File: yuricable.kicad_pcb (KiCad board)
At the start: 2 copper layers, 66.1 x 29.1 mm, 34 parts, among them U1 FlipperZero

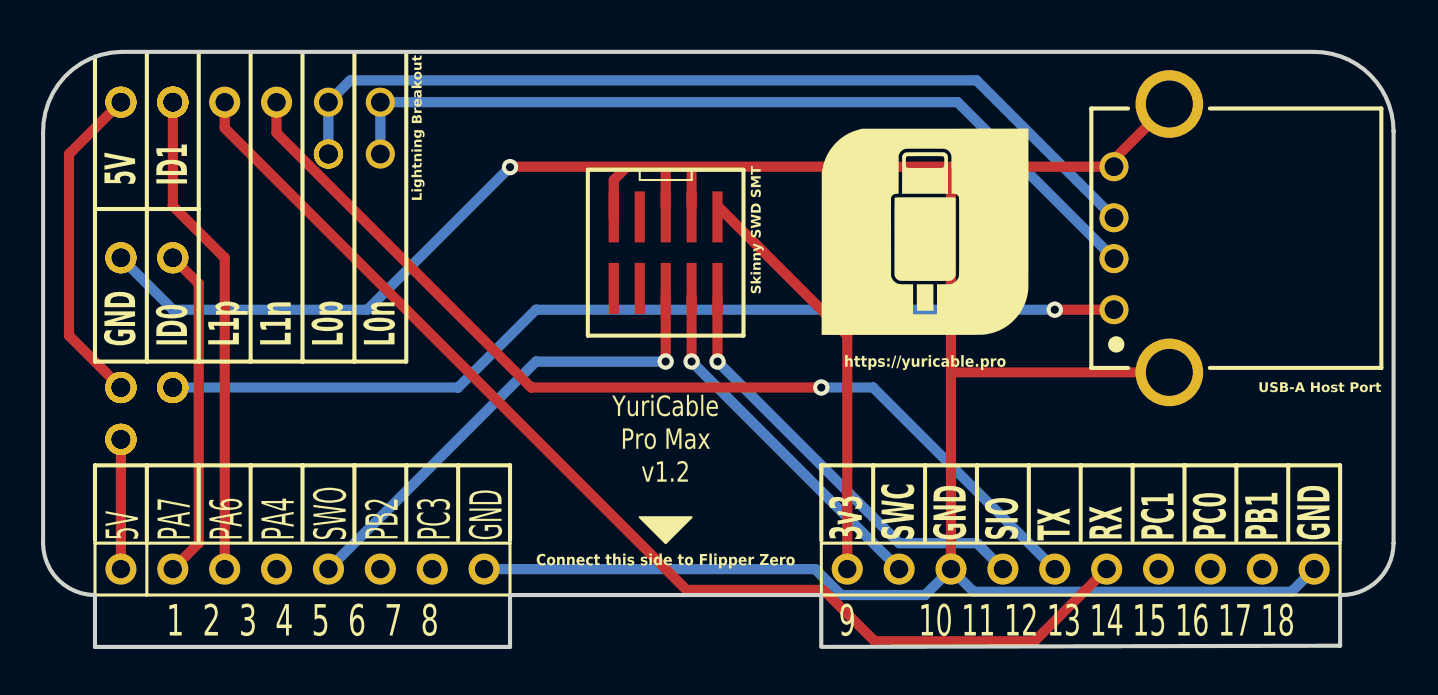
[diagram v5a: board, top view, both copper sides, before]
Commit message: rounded corners a bit more
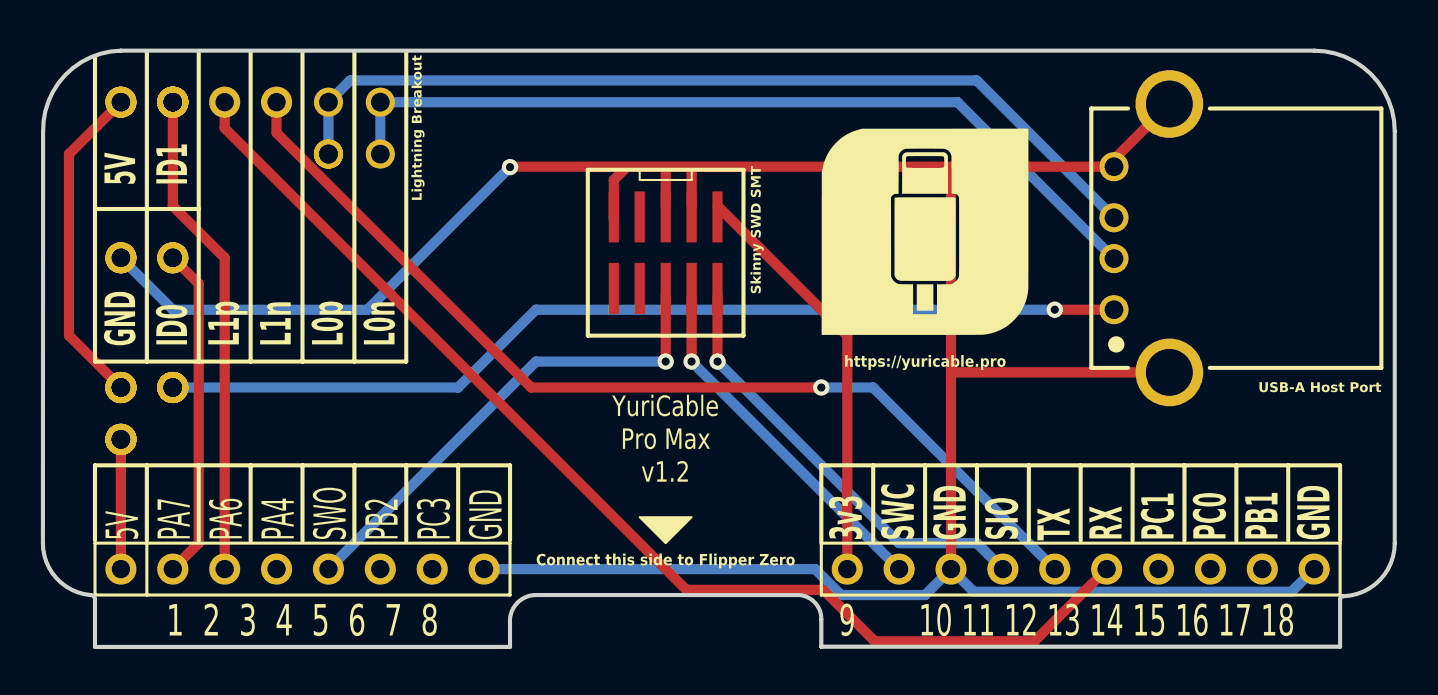
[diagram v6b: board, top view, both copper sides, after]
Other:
- board size 66.1 x 29.1 mm -> 66.2 x 29.2 mm
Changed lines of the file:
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@@
   (gr_line (start 123.19 71.12) (end 123.19 74.8)
     (stroke (width 0.2) (type solid)) (layer "F.SilkS"))
-  (gr_line (start 97.79 71.12) (end 97.79 74.8)
+  (gr_line (start 97.79 71.12) (end 97.79 74.93)
     (stroke (width 0.2) (type solid)) (layer "F.SilkS"))
   (gr_line (start 64.77 71.12) (end 64.77 74.8)
@@
   (gr_line (start 120.65 71.12) (end 120.65 74.8)
     (stroke (width 0.2) (type solid)) (layer "F.SilkS"))
-  (gr_arc (start 62.23 77.47) (mid 60.433949 76.726051) (end 59.69 74.93)
+  (gr_arc (start 62 77.47) (mid 60.347038 76.650161) (end 59.679608 74.93)
     (stroke (width 0.2) (type solid)) (layer "Edge.Cuts"))
-  (gr_arc (start 121.92 50.877038) (mid 124.668552 52.015525) (end 125.807039 54.764077)
+  (gr_arc (start 121.92 50.818141) (mid 124.710206 51.973878) (end 125.865959 54.764077)
     (stroke (width 0.2) (type solid)) (layer "Edge.Cuts"))
-  (gr_line (start 125.807039 74.93) (end 125.807039 54.764077)
+  (gr_line (start 125.865894 74.93) (end 125.865894 54.764077)
     (stroke (width 0.2) (type solid)) (layer "Edge.Cuts"))
   (gr_line (start 62.23 80.01) (end 82.55 80.01)
     (stroke (width 0.2) (type solid)) (layer "Edge.Cuts"))
-  (gr_line (start 63.5 50.877038) (end 121.92 50.877038)
+  (gr_line (start 63.5 50.818141) (end 121.92 50.818141)
     (stroke (width 0.2) (type solid)) (layer "Edge.Cuts"))
-  (gr_line (start 59.69 74.93) (end 59.69 54.841115)
+  (gr_line (start 59.679608 74.93) (end 59.69 54.782218)
     (stroke (width 0.2) (type solid)) (layer "Edge.Cuts"))
-  (gr_line (start 62.23 80.01) (end 62.23 77.585557)
+  (gr_line (start 62.23 80.01) (end 62.23 77.68)
     (stroke (width 0.2) (type solid)) (layer "Edge.Cuts"))
-  (gr_arc (start 59.69 54.841115) (mid 60.774013 52.07) (end 63.5 50.877038)
+  (gr_arc (start 59.69 54.782218) (mid 60.774014 52.011104) (end 63.5 50.818141)
     (stroke (width 0.2) (type solid)) (layer "Edge.Cuts"))
-  (gr_arc (start 125.807039 74.93) (mid 125.063091 76.726052) (end 123.267039 77.47)
+  (gr_arc (start 125.865894 74.93) (mid 125.131244 76.740744) (end 123.342635 77.527755)
     (stroke (width 0.2) (type solid)) (layer "Edge.Cuts"))
-  (gr_line (start 123.19 79.952221) (end 123.19 77.527778)
+  (gr_line (start 123.19 80) (end 123.19 77.686271)
     (stroke (width 0.2) (type solid)) (layer "Edge.Cuts"))
-  (gr_line (start 82.55 77.47) (end 97.79 77.47)
+  (gr_arc (start 62 77.47) (mid 62.158493 77.527365) (end 62.23 77.68)
     (stroke (width 0.2) (type solid)) (layer "Edge.Cuts"))
-  (gr_line (start 97.79 79.952221) (end 97.79 77.527778)
+  (gr_line (start 83.82 77.47) (end 96.560774 77.469998)
     (stroke (width 0.2) (type solid)) (layer "Edge.Cuts"))
-  (gr_line (start 97.79 80.01) (end 123.19 79.952221)
+  (gr_arc (start 123.19 77.686271) (mid 123.233487 77.575401) (end 123.342635 77.527756)
     (stroke (width 0.2) (type solid)) (layer "Edge.Cuts"))
-  (gr_line (start 82.55 80.01) (end 82.55 77.585557)
+  (gr_line (start 97.79 80) (end 97.79 78.667996)
+    (stroke (width 0.2) (type solid)) (layer "Edge.Cuts"))
+  (gr_arc (start 82.55 78.847043) (mid 82.882623 77.879728) (end 83.819918 77.470076)
+    (stroke (width 0.2) (type solid)) (layer "Edge.Cuts"))
+  (gr_line (start 97.79 80) (end 123.19 80)
+    (stroke (width 0.2) (type solid)) (layer "Edge.Cuts"))
+  (gr_arc (start 96.560692 77.470073) (mid 97.43837 77.799119) (end 97.79 78.667996)
+    (stroke (width 0.2) (type solid)) (layer "Edge.Cuts"))
+  (gr_line (start 82.55 80.01) (end 82.55 78.847043)
     (stroke (width 0.2) (type solid)) (layer "Edge.Cuts"))
   (image (at 218.44 171.45) (layer "F.Cu") (scale 0.314557)
